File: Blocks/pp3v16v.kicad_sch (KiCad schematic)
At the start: 33 parts, among them Q201 2N7002, U201 LM339

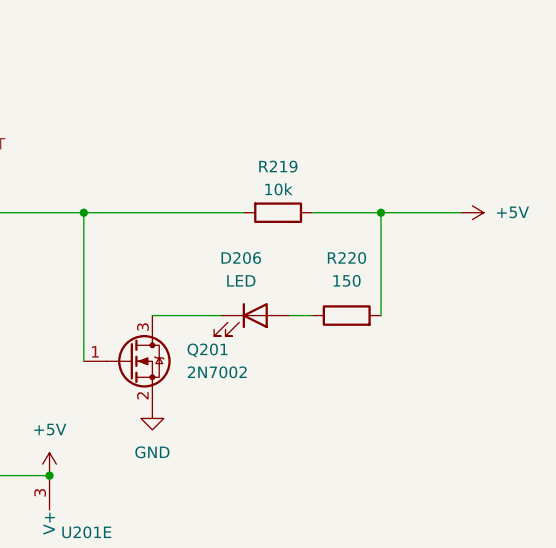
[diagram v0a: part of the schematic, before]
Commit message: add LED jumper
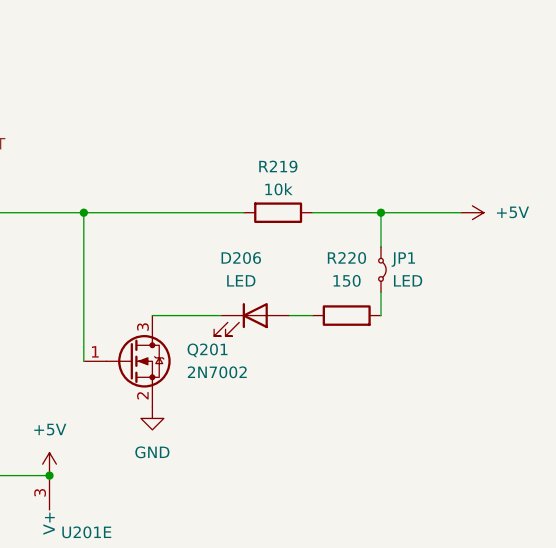
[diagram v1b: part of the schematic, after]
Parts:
- added JP1: LED, Connector_PinHeader_1.00mm:PinHeader_1x02_P1.00mm_Vertical, symbol Jumper:Jumper_2_Small_Bridged
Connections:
- net +5V: now also JP1.1 (A); no longer R220.2
- new net: JP1.2 (B), R220.2
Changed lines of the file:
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@@
 	(wire
 		(pts
-			(xy 212.09 40.64) (xy 212.09 52.07)
+			(xy 212.09 40.64) (xy 212.09 44.45)
 		)
 		(stroke
@@
 	(wire
 		(pts
+			(xy 212.09 49.53) (xy 212.09 52.07)
+		)
+		(stroke
+			(width 0)
+			(type default)
+		)
+	)
+	(wire
+		(pts
 			(xy 116.84 33.02) (xy 127 33.02)
 		)
@@
 					(unit 1)
 				)
+			)
+		)
+	)
+	(symbol
+		(lib_id "Jumper:Jumper_2_Small_Bridged")
+		(at 212.09 46.99 270)
+		(unit 1)
+		(exclude_from_sim yes)
+		(in_bom yes)
+		(on_board yes)
+		(dnp no)
+		(fields_autoplaced yes)
+		(property "Reference" "JP1"
+			(at 213.36 45.7199 90)
+			(effects
+				(font
+					(size 1.27 1.27)
+				)
+				(justify left)
+			)
+		)
+		(property "Value" "LED"
+			(at 213.36 48.2599 90)
+			(effects
+				(font
+					(size 1.27 1.27)
+				)
+				(justify left)
+			)
+		)
+		(property "Footprint" "Connector_PinHeader_1.00mm:PinHeader_1x02_P1.00mm_Vertical"
+			(at 212.09 46.99 0)
+			(effects
+				(font
+					(size 1.27 1.27)
+				)
+				(hide yes)
+			)
+		)
+		(property "Datasheet" "~"
+			(at 212.09 46.99 0)
+			(effects
+				(font
+					(size 1.27 1.27)
+				)
+				(hide yes)
+			)
+		)
+		(property "Description" "Jumper, 2-pole, small symbol, bridged"
+			(at 212.09 46.99 0)
+			(effects
+				(font
+					(size 1.27 1.27)
+				)
+				(hide yes)
+			)
+		)
+		(pin "2"
+		)
+		(pin "1"
+		)
+		(instances
+			(project ""
+				(path "/48ddfdd8-68fa-4e63-aa18-bc113cdf8cfa/542ec963-64f2-405e-acad-a2c979ff5c5c"
+					(reference "JP1")
+					(unit 1)
+				)

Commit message: clean up
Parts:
- removed D201, D202, D203, D205: LED, LED_SMD:LED_0603_1608Metric, symbol Device:LED
- removed R204, R207, R210, R216: 150, Resistor_SMD:R_0603_1608Metric, symbol Device:R
- removed R205: 5.6k, Resistor_SMD:R_0603_1608Metric, symbol Device:R
- removed R206, R209, R213, R218: 1k, Resistor_SMD:R_0603_1608Metric, symbol Device:R
- removed R208: 12k, Resistor_SMD:R_0603_1608Metric, symbol Device:R
- removed R212: 68k, Resistor_SMD:R_0603_1608Metric, symbol Device:R
- removed R217: 680k, Resistor_SMD:R_0603_1608Metric, symbol Device:R
- removed U201: LM339, Package_SO:SOIC-14_3.9x8.7mm_P1.27mm, symbol Comparator:LM339
- JP1: value LED -> JP1
